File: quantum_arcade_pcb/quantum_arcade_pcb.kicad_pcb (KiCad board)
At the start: 2 copper layers, 292.1 x 530.9 mm, 426 parts, among them J20 J20, Q10 2N3904, Q11 2N3904, Q12 2N3906, Q13 2N3904, Q14 2N3904, Q15 2N6044, Q16 2N6044, Q17 2N3904, Q7 2N3904, Q8 2N3906, Q9 2N3904, SW1 SW_DIP_x08, SW2 SW_DIP_x08, Y1 12.096MHz

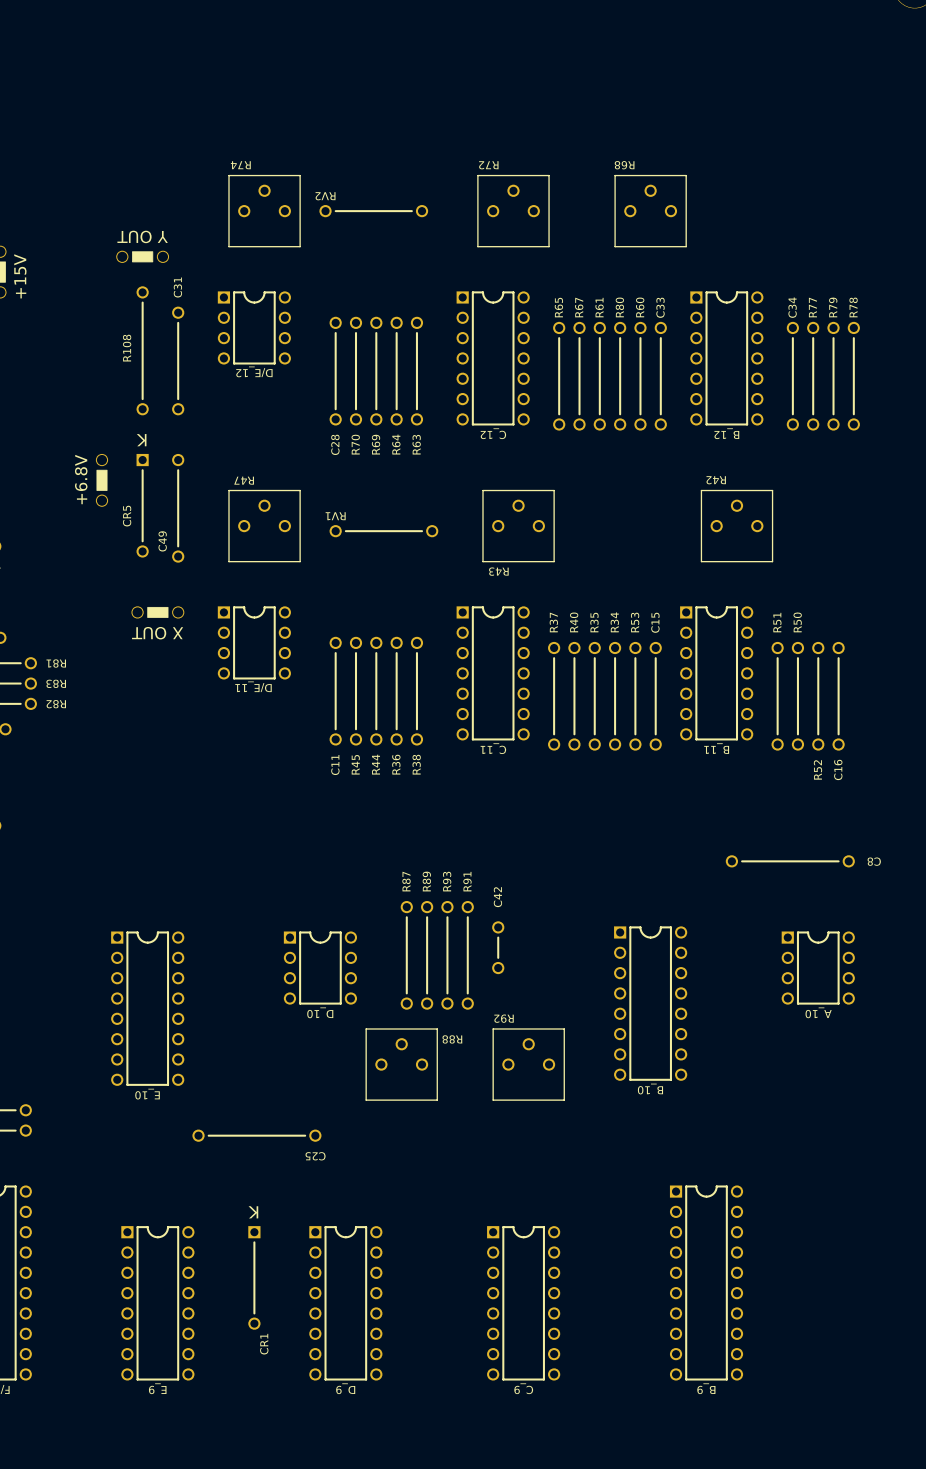
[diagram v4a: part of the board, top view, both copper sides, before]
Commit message: 25 components left to place
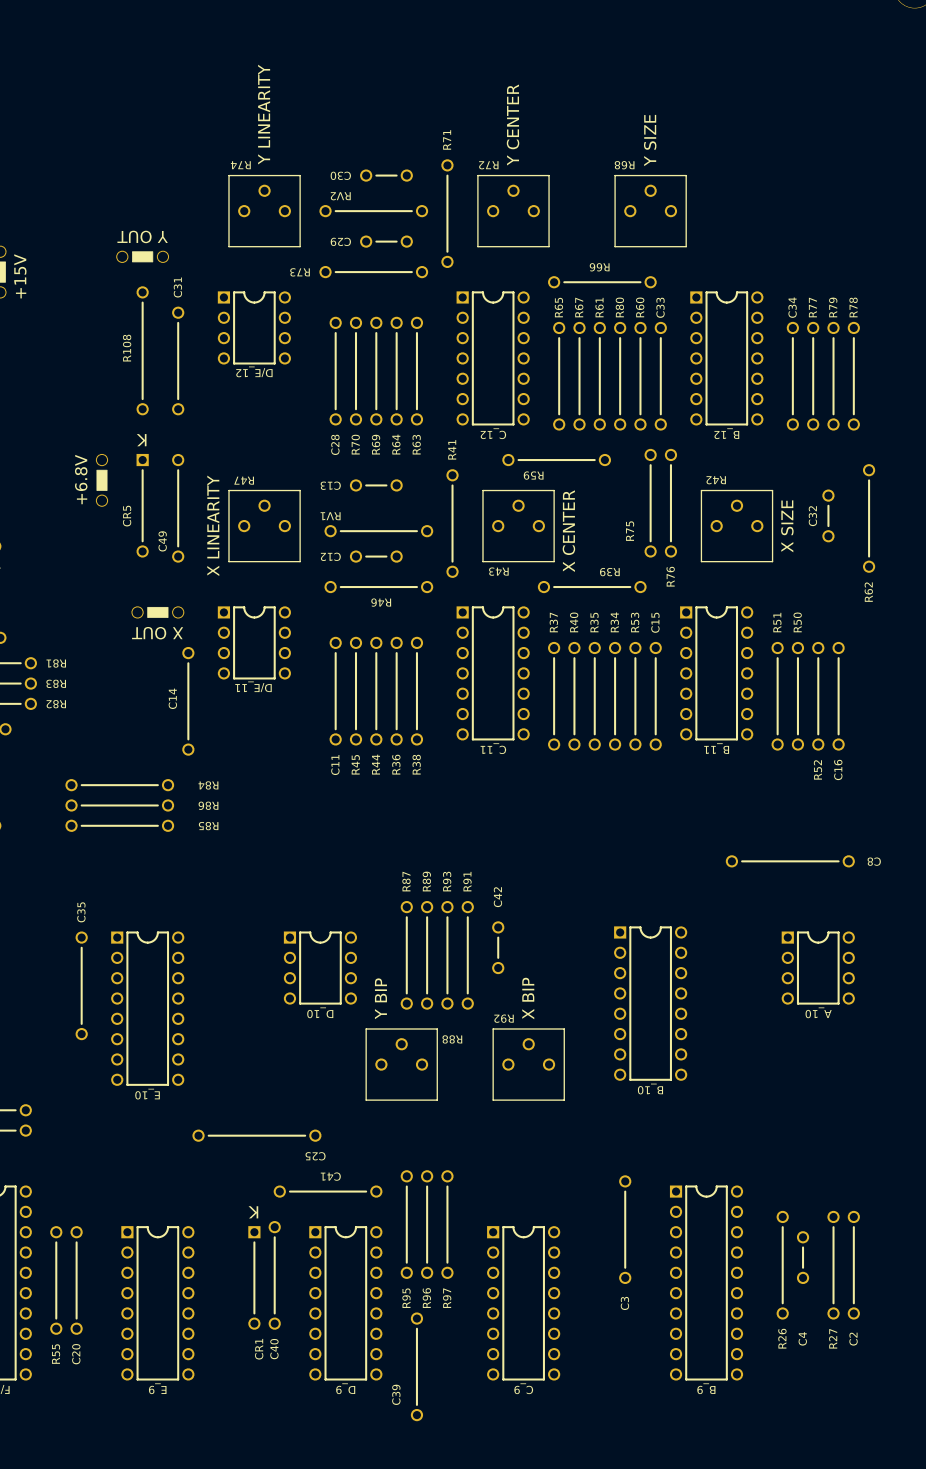
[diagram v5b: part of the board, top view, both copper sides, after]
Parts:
- added C12: 39pf, quantum_arcade_pcb:CapSmall, F.Cu at (243.2, 113.0)
- added C13: 100pf, quantum_arcade_pcb:CapSmall, F.Cu at (243.2, 104.1)
- added C14: .1uF, quantum_arcade_pcb:GenComp, F.Cu at (219.7, 131.4)
- added C2: .1uF, quantum_arcade_pcb:GenComp, F.Cu at (302.9, 201.3)
- added C20: .1uF, quantum_arcade_pcb:GenComp, F.Cu at (205.7, 203.8)
- added C29: 39pf, quantum_arcade_pcb:CapSmall, F.Cu at (244.5, 73.7)
- added C3: .1uF, quantum_arcade_pcb:GenComp, F.Cu at (274.3, 197.5)
- added C30: 100pf, quantum_arcade_pcb:CapSmall, F.Cu at (244.5, 65.4)
- added C32: 100pf, quantum_arcade_pcb:CapSmall, F.Cu at (299.7, 108.0)
- added C35: .1uF, quantum_arcade_pcb:GenComp, F.Cu at (206.4, 167.0)
- added C39: .1uF, quantum_arcade_pcb:GenComp, F.Cu at (248.3, 214.6)
- added C4: .01uF, quantum_arcade_pcb:CapSmall, F.Cu at (296.5, 200.7)
- added C40: .1uF, quantum_arcade_pcb:GenComp, F.Cu at (230.5, 202.6)
- added C41: .01uF, quantum_arcade_pcb:GenComp, F.Cu at (236.9, 192.4)
- added R26: 820, quantum_arcade_pcb:GenComp, F.Cu at (294.0, 201.9)
- added R27: 820, quantum_arcade_pcb:GenComp, F.Cu at (300.4, 201.3)
- added R39: 3.9k, quantum_arcade_pcb:GenComp, F.Cu at (270.5, 116.8)
- added R41: 5.6k, quantum_arcade_pcb:GenComp, F.Cu at (252.7, 108.6)
- added R46: 10k, quantum_arcade_pcb:GenComp, F.Cu at (243.2, 116.8)
- added R55: 820, quantum_arcade_pcb:GenComp, F.Cu at (203.2, 203.2)
- added R59: 470, quantum_arcade_pcb:GenComp, F.Cu at (265.4, 101.0)
- added R62: 470, quantum_arcade_pcb:GenComp, F.Cu at (304.8, 108.0)
- added R66: 3.9k, quantum_arcade_pcb:GenComp, F.Cu at (271.8, 78.7)
- added R71: 5.6k, quantum_arcade_pcb:GenComp, F.Cu at (252.1, 69.8)
- added R73: 10k, quantum_arcade_pcb:GenComp, F.Cu at (242.6, 77.5)
- added R75: 100k, quantum_arcade_pcb:GenComp, F.Cu at (277.5, 106.7)
- added R76: 1.2k, quantum_arcade_pcb:GenComp, F.Cu at (280.0, 106.7)
- added R84: 560, quantum_arcade_pcb:GenComp, F.Cu at (211.5, 141.6)
- added R85: 7.5K, quantum_arcade_pcb:GenComp, F.Cu at (211.5, 146.7)
- added R86: 7.5K, quantum_arcade_pcb:GenComp, F.Cu at (211.5, 144.1)
- added R95: 7.5K, quantum_arcade_pcb:GenComp, F.Cu at (247.0, 196.2)
- added R96: 7.5K, quantum_arcade_pcb:GenComp, F.Cu at (249.6, 196.2)
- added R97: 3.9K, quantum_arcade_pcb:GenComp, F.Cu at (252.1, 196.2)
- moved RV1 0.63 mm to (243.2, 109.9)
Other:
- board text added: "X BIP"
- board text added: "X CENTER"
- board text added: "X LINEARITY"
- board text added: "X SIZE"
- board text added: "Y BIP"
- board text added: "Y CENTER"
- board text added: "Y LINEARITY"
- board text added: "Y SIZE"

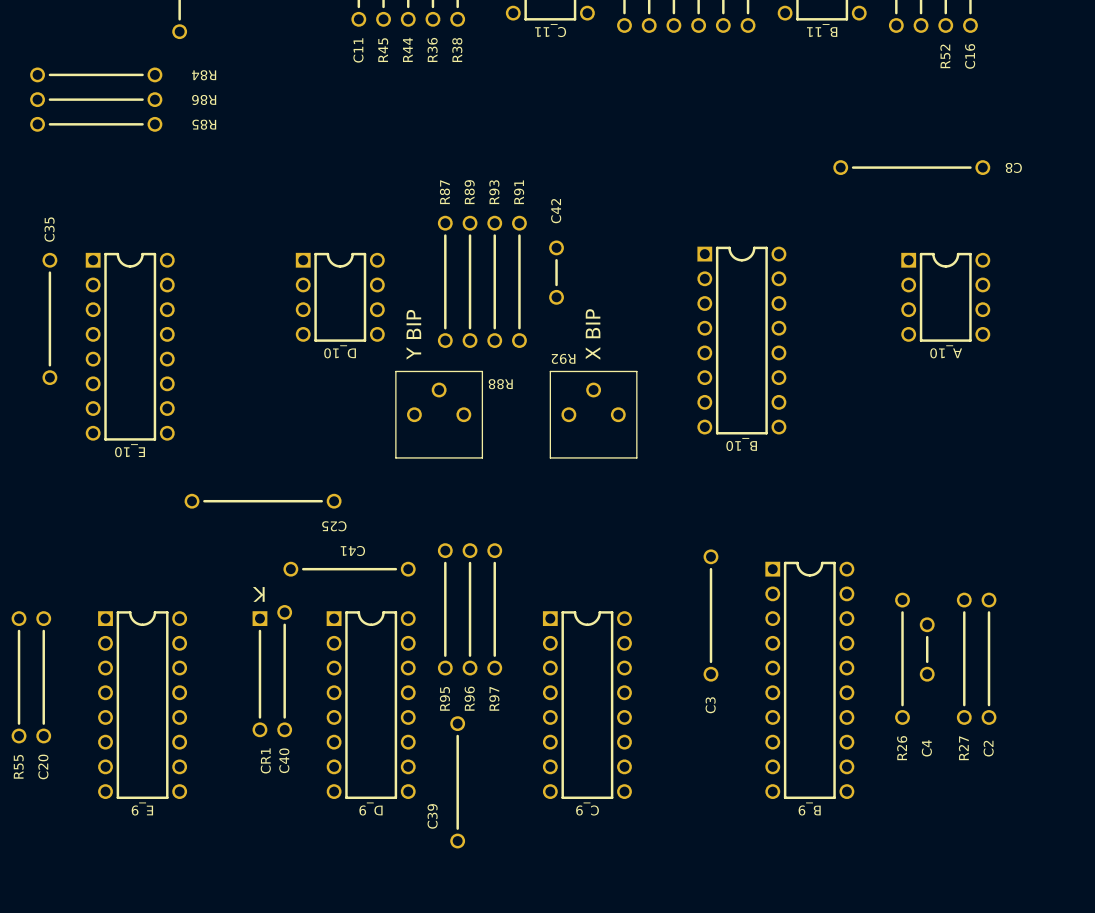
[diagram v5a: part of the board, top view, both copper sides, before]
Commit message: Finished placing components
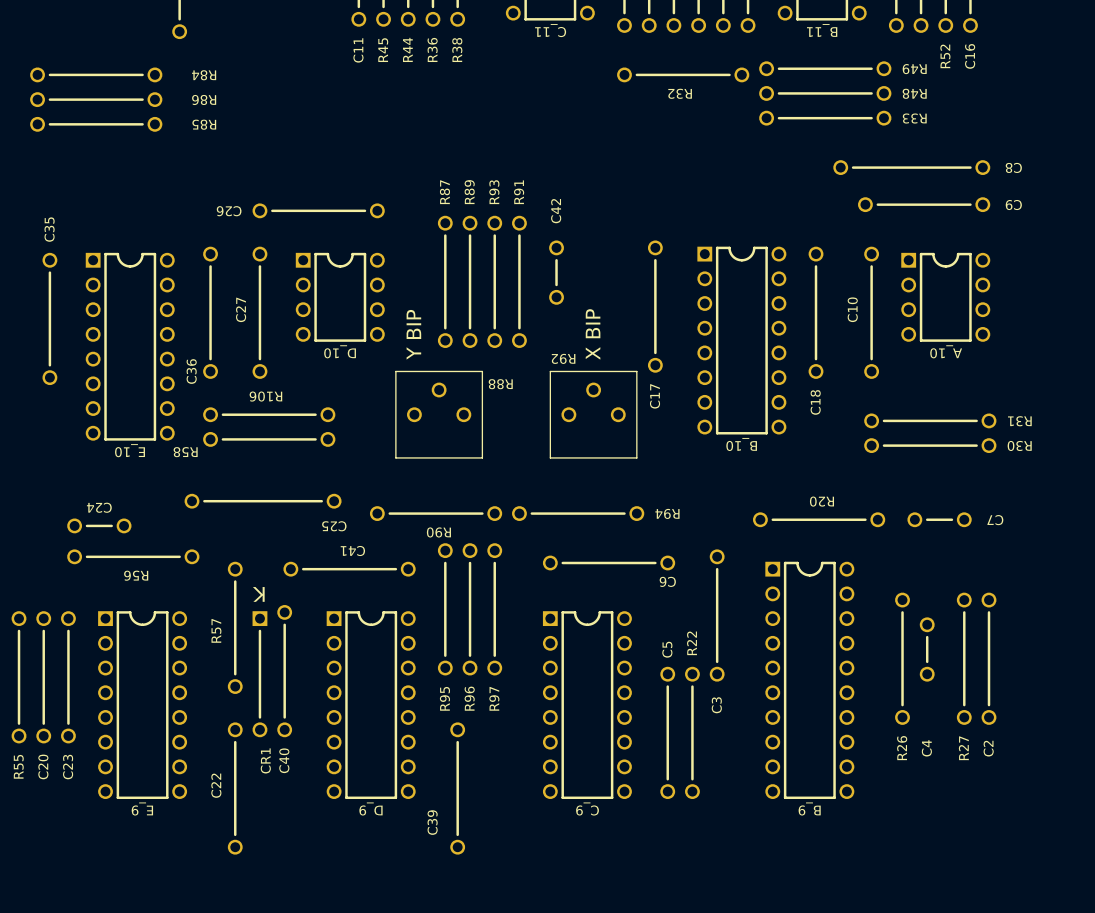
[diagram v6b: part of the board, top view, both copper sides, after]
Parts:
- added C10: .1uF, quantum_arcade_pcb:GenComp, F.Cu at (290.8, 165.7)
- added C17: .1uF, quantum_arcade_pcb:GenComp, F.Cu at (268.6, 165.7)
- added C18: .1uF, quantum_arcade_pcb:GenComp, F.Cu at (285.1, 166.4)
- added C22: ?, quantum_arcade_pcb:GenComp, F.Cu at (225.4, 214.6)
- added C23: ?, quantum_arcade_pcb:GenComp, F.Cu at (208.3, 203.8)
- added C24: ?, quantum_arcade_pcb:CapSmall, F.Cu at (211.5, 188.0)
- added C26: .1uF, quantum_arcade_pcb:GenComp, F.Cu at (233.7, 155.6)
- added C27: .1uF, quantum_arcade_pcb:GenComp, F.Cu at (228.0, 165.7)
- added C36: .1uF, quantum_arcade_pcb:GenComp, F.Cu at (222.9, 165.7)
- added C5: ?, quantum_arcade_pcb:GenComp, F.Cu at (269.9, 208.9)
- added C6: ?, quantum_arcade_pcb:GenComp, F.Cu at (263.5, 191.8)
- added C7: ?, quantum_arcade_pcb:CapSmall, F.Cu at (297.8, 187.3)
- added C9: .1uF, quantum_arcade_pcb:GenComp, F.Cu at (295.9, 154.9)
- added R106: 7.5K, quantum_arcade_pcb:GenComp, F.Cu at (229.2, 176.5)
- added R20: ?, quantum_arcade_pcb:GenComp, F.Cu at (285.8, 187.3)
- added R22: ?, quantum_arcade_pcb:GenComp, F.Cu at (272.4, 209.6)
- added R30: 7.5K, quantum_arcade_pcb:GenComp, F.Cu at (296.5, 179.7)
- added R31: 7.5K, quantum_arcade_pcb:GenComp, F.Cu at (297.2, 177.2)
- added R32: 470, quantum_arcade_pcb:GenComp, F.Cu at (271.1, 141.6)
- added R33: 470, quantum_arcade_pcb:GenComp, F.Cu at (286.4, 146.1)
- added R48: 100k, quantum_arcade_pcb:GenComp, F.Cu at (285.8, 143.5)
- added R49: 1.5k, quantum_arcade_pcb:GenComp, F.Cu at (285.8, 141.0)
- added R56: ?, quantum_arcade_pcb:GenComp, F.Cu at (214.6, 191.1)
- added R57: ?, quantum_arcade_pcb:GenComp, F.Cu at (225.4, 198.1)
- added R58: 7.5K, quantum_arcade_pcb:GenComp, F.Cu at (228.6, 179.1)
- added R90: 100, quantum_arcade_pcb:GenComp, F.Cu at (245.7, 186.7)
- added R94: 100, quantum_arcade_pcb:GenComp, F.Cu at (261.0, 186.7)
- moved C3 0.63 mm to (275.0, 197.5)
- moved C39 0.63 mm to (248.3, 215.3)
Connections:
- C_9 pad 1: Net-(C_9-Pad1) -> -15V
- C_9 pad 10: Net-(C_9-Pad10) -> DVX5
- C_9 pad 11: Net-(C_9-Pad11) -> DVX4
- C_9 pad 12: Net-(C_9-Pad12) -> DVX3
- C_9 pad 13: Net-(C_9-Pad13) -> DVX2
- C_9 pad 14: Net-(C_9-Pad14) -> +5V
- C_9 pad 16: Net-(C_9-Pad16) -> XREF
- C_9 pad 2: Net-(C_9-Pad2) -> GND
- C_9 pad 3: Net-(C_9-Pad3) -> YBIP
- C_9 pad 4: Net-(C_9-Pad4) -> ~DVX11
- C_9 pad 5: Net-(C_9-Pad5) -> DVX10
- C_9 pad 6: Net-(C_9-Pad6) -> DVX9
- C_9 pad 7: Net-(C_9-Pad7) -> DVX8
- C_9 pad 8: Net-(C_9-Pad8) -> DVX7
- C_9 pad 9: Net-(C_9-Pad9) -> DVX6
- E_9 pad 1: Net-(E_9-Pad1) -> -15V
- E_9 pad 10: Net-(E_9-Pad10) -> DVY5
- E_9 pad 11: Net-(E_9-Pad11) -> DVY4
- E_9 pad 12: Net-(E_9-Pad12) -> DVY3
- E_9 pad 13: Net-(E_9-Pad13) -> DVY2
- E_9 pad 14: Net-(E_9-Pad14) -> +5V
- E_9 pad 16: Net-(E_9-Pad16) -> YREF
- E_9 pad 2: Net-(E_9-Pad2) -> GND
- E_9 pad 3: Net-(E_9-Pad3) -> XBIP
- E_9 pad 4: Net-(E_9-Pad4) -> ~DVY11
- E_9 pad 5: Net-(E_9-Pad5) -> DVY10
- E_9 pad 6: Net-(E_9-Pad6) -> DVY9
- E_9 pad 7: Net-(E_9-Pad7) -> DVY8
- E_9 pad 8: Net-(E_9-Pad8) -> DVY7
- E_9 pad 9: Net-(E_9-Pad9) -> DVY6

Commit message: 1498 disconnected signals remain
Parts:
- J20: footprint Asteroids:J20 -> quantum_arcade_pcb:EdgeCon
- moved J20 53.3 mm to (130.2, 56.5)
- moved C77 0.64 mm to (37.5, 249.6)
- moved R177 0.64 mm to (40.0, 262.3)
- moved R214 0.64 mm to (80.0, 125.1)
- moved C76 0.63 mm to (41.3, 249.6)
- moved L1 0.63 mm to (45.1, 248.3)
- moved R172 0.63 mm to (40.0, 439.4), turned to 0 degrees
- moved R178 0.63 mm to (39.4, 259.7)
- moved R179 0.63 mm to (39.4, 239.4)
- moved C46 0.63 mm to (148.6, 77.5), turned to 180 degrees
- moved C96 0.63 mm to (39.4, 541.0)
- moved M_2 0.63 mm to (102.9, 499.7)
- moved N_2 0.63 mm to (80.0, 499.7)
- moved P_1 0.63 mm to (53.3, 546.1)
- moved P_2 0.63 mm to (53.3, 501.0)
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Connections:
- C71 pad 2: GND -> +5V
- C_9 pad 3: YBIP -> XBIP
- E_9 pad 3: XBIP -> YBIP
- Y1 pad 1: Net-(C76-Pad1) -> GND
- Y1 pad 2: GND -> Net-(C76-Pad1)
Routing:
- net GND: track 0.00 -> 5971.1 mm, vias 0 -> 15
- net +5V: track 23.5 -> 5060.7 mm, vias 1 -> 17
- net R\~W~B: track 0.00 -> 201.9 mm, vias 0 -> 2
- net MB14: track 0.00 -> 201.3 mm
- net MB15: track 0.00 -> 201.3 mm
- net MB13: track 0.00 -> 198.8 mm
- net MB4: track 0.00 -> 196.9 mm
- net MB12: track 0.00 -> 196.2 mm
- net MB3: track 0.00 -> 194.3 mm
- net MB11: track 0.00 -> 193.7 mm
- net MB8: track 0.00 -> 183.5 mm
- net MB9: track 0.00 -> 181.0 mm
- net A23: track 0.00 -> 179.1 mm, vias 0 -> 1
- net MB2: track 0.00 -> 179.1 mm
- net MB10: track 0.00 -> 178.4 mm
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- added copper zone on B.Cu, net GND
- added copper zone on F.Cu, net GND

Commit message: Added more traces
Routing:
- net R\~W: track 0.00 -> 411.5 mm, vias 0 -> 4
- net ~VPA: track 0.00 -> 335.3 mm, vias 0 -> 3
- net ~AS: track 0.00 -> 320.0 mm, vias 0 -> 3
- net PR218: track 63.5 -> 375.3 mm, vias 1 -> 3
- net FC0: track 0.00 -> 226.1 mm, vias 0 -> 2
- net ~VMEM: track 0.00 -> 221.0 mm, vias 0 -> 1
- net A23: track 179.1 -> 389.9 mm, vias 1 -> 3
- net FC2: track 0.00 -> 200.7 mm, vias 0 -> 2
- net FC1: track 0.00 -> 199.6 mm, vias 0 -> 2
- net A19: track 0.00 -> 188.0 mm, vias 0 -> 2
- net A18: track 0.00 -> 188.0 mm, vias 0 -> 2
- net A21: track 0.00 -> 186.7 mm, vias 0 -> 2
- net ~IRQ: track 0.00 -> 186.1 mm, vias 0 -> 2
- net A20: track 0.00 -> 184.2 mm, vias 0 -> 2
- net GND: track 5971.1 -> 6153.4 mm
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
